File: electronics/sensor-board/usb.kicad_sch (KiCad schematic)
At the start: 1 part

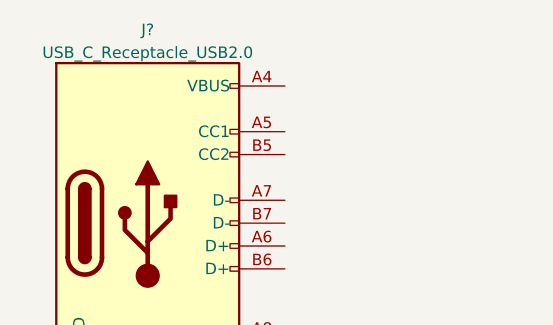
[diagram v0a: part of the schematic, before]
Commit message: Upload power supply schematic
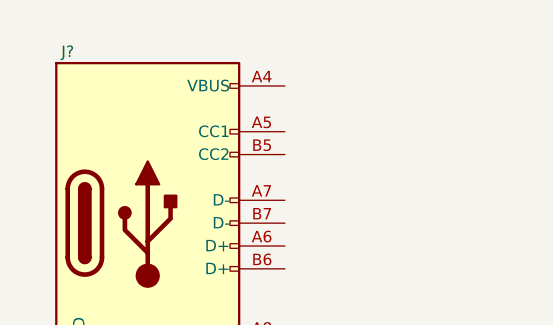
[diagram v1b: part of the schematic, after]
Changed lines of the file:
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@@
   )
   (symbol (lib_id "Connector:USB_C_Receptacle_USB2.0") (at 99.06 76.2 0) (unit 1)
-    (in_bom yes) (on_board yes) (fields_autoplaced)
-    (property "Reference" "J?" (id 0) (at 99.06 54.7202 0))
-    (property "Value" "USB_C_Receptacle_USB2.0" (id 1) (at 99.06 57.2571 0))
+    (in_bom yes) (on_board yes)
+    (property "Reference" "J?" (id 0) (at 90.17 57.15 0))
+    (property "Value" "USB_C_Receptacle_USB2.0" (id 1) (at 99.06 57.2571 0)
+      (effects (font (size 1.27 1.27)) hide)
+    )
     (property "Footprint" "" (id 2) (at 102.87 76.2 0)
       (effects (font (size 1.27 1.27)) hide)

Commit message: Finalize USB
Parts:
- added R?: 1.5k, symbol Device:R_Small
- added R? (x2): 5.1k, symbol Device:R_Small
- added R? (x2): 22R, symbol Device:R_Small
- added TP?: TestPoint, symbol Connector:TestPoint
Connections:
- net USB_DM: now also R?.2
- net USB_DP: now also R?.2
- net GND: now reaches J?.A1 (GND), J?.A12 (GND), J?.B1 (GND), J?.B12 (GND)
- net GND: now also J?.S1 (SHIELD), R?.2, R?.2
- net VBUS: now reaches J?.A4 (VBUS), J?.A9 (VBUS), J?.B4 (VBUS), J?.B9 (VBUS)
- net VBUS: now also TP?.1
- net at J?.A5 (CC1): now also R?.1
- net at J?.A6 (D+): now also J?.B6 (D+), R?.1
- net at J?.A7 (D-): now also J?.B7 (D-), R?.1, R?.1
- net at J?.B5 (CC2): now also R?.1
- new net +3.3V: R?.2
- no-connect marks 0 -> 2
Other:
- note added: "USB for debug, programming and PC data (not a power supply)"
- moved on the sheet: J?

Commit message: Build Pad Bus and annotate
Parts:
- removed TP?: TestPoint, symbol Connector:TestPoint
- gave numbers to parts that had none: 6
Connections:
- net VBUS: no longer names the net of J18.A4 (VBUS), J18.A9 (VBUS), J18.B4 (VBUS), J18.B9 (VBUS)
- no-connect marks 2 -> 3
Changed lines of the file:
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@@
 (kicad_sch (version 20211123) (generator eeschema)
   (paper "A4")
-  (junction (at 52.07 29.21) (diameter 0) (color 0 0 0 0)
-  )
-  (junction (at 60.96 29.21) (diameter 0) (color 0 0 0 0)
-  )
   (junction (at 48.26 41.91) (diameter 0) (color 0 0 0 0)
   )
@@
   (junction (at 48.26 46.99) (diameter 0) (color 0 0 0 0)
   )
+  (no_connect (at 45.72 29.21))
   (no_connect (at 45.72 57.15))
   (no_connect (at 45.72 59.69))
@@
     (stroke (width 0) (type default) (color 0 0 0 0))
   )
-  (wire (pts (xy 52.07 26.67) (xy 52.07 29.21))
-    (stroke (width 0) (type default) (color 0 0 0 0))
-  )
-  (wire (pts (xy 67.31 29.21) (xy 60.96 29.21))
-    (stroke (width 0) (type default) (color 0 0 0 0))
-  )
   (wire (pts (xy 45.72 46.99) (xy 48.26 46.99))
     (stroke (width 0) (type default) (color 0 0 0 0))
@@
     (stroke (width 0) (type default) (color 0 0 0 0))
   )
-  (wire (pts (xy 60.96 29.21) (xy 60.96 26.67))
-    (stroke (width 0) (type default) (color 0 0 0 0))
-  )
-  (wire (pts (xy 67.31 27.94) (xy 67.31 29.21))
-    (stroke (width 0) (type default) (color 0 0 0 0))
-  )
   (wire (pts (xy 48.26 46.99) (xy 48.26 49.53))
     (stroke (width 0) (type default) (color 0 0 0 0))
@@
     (stroke (width 0) (type default) (color 0 0 0 0))
   )
-  (wire (pts (xy 52.07 29.21) (xy 60.96 29.21))
-    (stroke (width 0) (type default) (color 0 0 0 0))
-  )
   (wire (pts (xy 22.86 69.85) (xy 22.86 71.12))
     (stroke (width 0) (type default) (color 0 0 0 0))
@@
   )
   (wire (pts (xy 48.26 49.53) (xy 45.72 49.53))
-    (stroke (width 0) (type default) (color 0 0 0 0))
-  )
-  (wire (pts (xy 45.72 29.21) (xy 52.07 29.21))
     (stroke (width 0) (type default) (color 0 0 0 0))
   )
@@
   (symbol (lib_id "power:GND") (at 72.39 38.1 0) (unit 1)
     (in_bom yes) (on_board yes) (fields_autoplaced)
-    (property "Reference" "#PWR?" (id 0) (at 72.39 44.45 0)
+    (property "Reference" "#PWR0103" (id 0) (at 72.39 44.45 0)
       (effects (font (size 1.27 1.27)) hide)
     )
@@
     (pin "1")
   )
-  (symbol (lib_id "power:VBUS") (at 52.07 26.67 0) (unit 1)
-    (in_bom yes) (on_board yes) (fields_autoplaced)
-    (property "Reference" "#PWR?" (id 0) (at 52.07 30.48 0)
-      (effects (font (size 1.27 1.27)) hide)
-    )
-    (property "Value" "VBUS" (id 1) (at 52.07 23.0942 0))
-    (property "Footprint" "" (id 2) (at 52.07 26.67 0)
-      (effects (font (size 1.27 1.27)) hide)
-    )
-    (property "Datasheet" "" (id 3) (at 52.07 26.67 0)
-      (effects (font (size 1.27 1.27)) hide)
-    )
-    (pin "1")
-  )
   (symbol (lib_id "Device:R_Small") (at 52.07 39.37 90) (unit 1)
     (in_bom yes) (on_board yes)
-    (property "Reference" "R?" (id 0) (at 55.88 40.64 90))
+    (property "Reference" "R56" (id 0) (at 55.88 40.64 90))
     (property "Value" "1.5k" (id 1) (at 57.15 38.1 90))
     (property "Footprint" "" (id 2) (at 52.07 39.37 0)
@@
   (symbol (lib_id "Device:R_Small") (at 52.07 36.83 90) (unit 1)
     (in_bom yes) (on_board yes)
-    (property "Reference" "R?" (id 0) (at 48.26 35.56 90))
+    (property "Reference" "R55" (id 0) (at 48.26 35.56 90))
     (property "Value" "5.1k" (id 1) (at 57.15 35.56 90))
     (property "Footprint" "" (id 2) (at 52.07 36.83 0)
@@
   (symbol (lib_id "power:+3.3V") (at 63.5 38.1 0) (unit 1)
     (in_bom yes) (on_board yes)
-    (property "Reference" "#PWR?" (id 0) (at 63.5 41.91 0)
+    (property "Reference" "#PWR0102" (id 0) (at 63.5 41.91 0)
       (effects (font (size 1.27 1.27)) hide)
     )
@@
     (pin "1")
   )
-  (symbol (lib_id "Connector:TestPoint") (at 67.31 27.94 0) (unit 1)
-    (in_bom yes) (on_board yes) (fields_autoplaced)
-    (property "Reference" "TP?" (id 0) (at 68.707 23.8033 0)
-      (effects (font (size 1.27 1.27)) (justify left))
-    )
-    (property "Value" "TestPoint" (id 1) (at 68.707 26.3402 0)
-      (effects (font (size 1.27 1.27)) (justify left))
-    )
-    (property "Footprint" "" (id 2) (at 72.39 27.94 0)
-      (effects (font (size 1.27 1.27)) hide)
-    )
-    (property "Datasheet" "~" (id 3) (at 72.39 27.94 0)
-      (effects (font (size 1.27 1.27)) hide)
-    )
-    (pin "1")
-  )
   (symbol (lib_id "Connector:USB_C_Receptacle_USB2.0") (at 30.48 44.45 0) (unit 1)
     (in_bom yes) (on_board yes)
-    (property "Reference" "J?" (id 0) (at 21.59 25.4 0))
+    (property "Reference" "J18" (id 0) (at 21.59 25.4 0))
     (property "Value" "USB_C_Receptacle_USB2.0" (id 1) (at 30.48 25.5071 0)
       (effects (font (size 1.27 1.27)) hide)
@@
   (symbol (lib_id "Device:R_Small") (at 52.07 34.29 90) (unit 1)
     (in_bom yes) (on_board yes)
-    (property "Reference" "R?" (id 0) (at 48.26 33.02 90))
+    (property "Reference" "R54" (id 0) (at 48.26 33.02 90))
     (property "Value" "5.1k" (id 1) (at 57.15 33.02 90))
     (property "Footprint" "" (id 2) (at 52.07 34.29 0)
@@
   (symbol (lib_id "power:GND") (at 22.86 71.12 0) (unit 1)
     (in_bom yes) (on_board yes) (fields_autoplaced)
-    (property "Reference" "#PWR?" (id 0) (at 22.86 77.47 0)
+    (property "Reference" "#PWR0101" (id 0) (at 22.86 77.47 0)
       (effects (font (size 1.27 1.27)) hide)
     )
@@
     (pin "1")
   )
-  (symbol (lib_id "power:PWR_FLAG") (at 60.96 26.67 0) (unit 1)
-    (in_bom yes) (on_board yes) (fields_autoplaced)
-    (property "Reference" "#FLG?" (id 0) (at 60.96 24.765 0)
-      (effects (font (size 1.27 1.27)) hide)
-    )
-    (property "Value" "PWR_FLAG" (id 1) (at 60.96 23.0942 0))
-    (property "Footprint" "" (id 2) (at 60.96 26.67 0)
-      (effects (font (size 1.27 1.27)) hide)
-    )
-    (property "Datasheet" "~" (id 3) (at 60.96 26.67 0)
-      (effects (font (size 1.27 1.27)) hide)
-    )
-    (pin "1")
-  )
   (symbol (lib_id "Device:R_Small") (at 52.07 46.99 90) (unit 1)
     (in_bom yes) (on_board yes)
-    (property "Reference" "R?" (id 0) (at 55.88 48.26 90))
+    (property "Reference" "R58" (id 0) (at 55.88 48.26 90))
     (property "Value" "22R" (id 1) (at 52.07 49.53 90))
     (property "Footprint" "" (id 2) (at 52.07 46.99 0)
@@
   (symbol (lib_id "Device:R_Small") (at 52.07 41.91 90) (unit 1)
     (in_bom yes) (on_board yes)
-    (property "Reference" "R?" (id 0) (at 55.88 43.18 90))
+    (property "Reference" "R57" (id 0) (at 55.88 43.18 90))
     (property "Value" "22R" (id 1) (at 52.07 44.45 90))
     (property "Footprint" "" (id 2) (at 52.07 41.91 0)

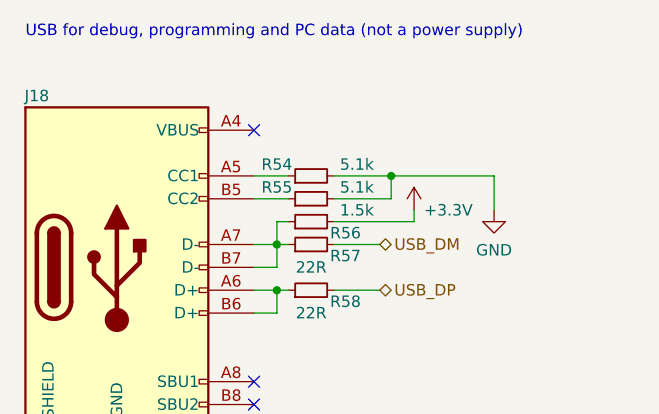
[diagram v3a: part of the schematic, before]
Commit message: Minor tweaks, footprints added
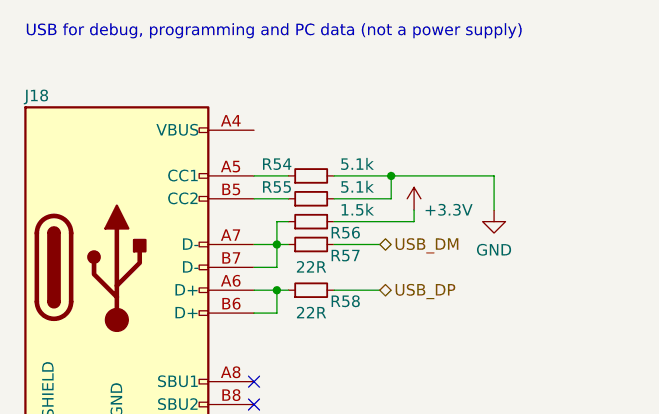
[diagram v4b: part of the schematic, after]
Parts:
- J18: footprint (none) -> Connector_USB:USB_C_Receptacle_Palconn_UTC16-G
- R54, R55, R56, R57, R58: footprint (none) -> Resistor_SMD:R_0603_1608Metric
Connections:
- no-connect marks 3 -> 2
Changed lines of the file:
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@@
   (junction (at 48.26 46.99) (diameter 0) (color 0 0 0 0)
   )
-  (no_connect (at 45.72 29.21))
   (no_connect (at 45.72 57.15))
   (no_connect (at 45.72 59.69))
@@
     (property "Reference" "R56" (id 0) (at 55.88 40.64 90))
     (property "Value" "1.5k" (id 1) (at 57.15 38.1 90))
-    (property "Footprint" "" (id 2) (at 52.07 39.37 0)
+    (property "Footprint" "Resistor_SMD:R_0603_1608Metric" (id 2) (at 52.07 39.37 0)
       (effects (font (size 1.27 1.27)) hide)
     )
@@
     (property "Reference" "R55" (id 0) (at 48.26 35.56 90))
     (property "Value" "5.1k" (id 1) (at 57.15 35.56 90))
-    (property "Footprint" "" (id 2) (at 52.07 36.83 0)
+    (property "Footprint" "Resistor_SMD:R_0603_1608Metric" (id 2) (at 52.07 36.83 0)
       (effects (font (size 1.27 1.27)) hide)
     )
@@
       (effects (font (size 1.27 1.27)) hide)
     )
-    (property "Footprint" "" (id 2) (at 34.29 44.45 0)
+    (property "Footprint" "Connector_USB:USB_C_Receptacle_Palconn_UTC16-G" (id 2) (at 34.29 44.45 0)
       (effects (font (size 1.27 1.27)) hide)
     )
@@
     (property "Reference" "R54" (id 0) (at 48.26 33.02 90))
     (property "Value" "5.1k" (id 1) (at 57.15 33.02 90))
-    (property "Footprint" "" (id 2) (at 52.07 34.29 0)
+    (property "Footprint" "Resistor_SMD:R_0603_1608Metric" (id 2) (at 52.07 34.29 0)
       (effects (font (size 1.27 1.27)) hide)
     )
@@
     (property "Reference" "R58" (id 0) (at 55.88 48.26 90))
     (property "Value" "22R" (id 1) (at 52.07 49.53 90))
-    (property "Footprint" "" (id 2) (at 52.07 46.99 0)
+    (property "Footprint" "Resistor_SMD:R_0603_1608Metric" (id 2) (at 52.07 46.99 0)
       (effects (font (size 1.27 1.27)) hide)
     )
@@
     (property "Reference" "R57" (id 0) (at 55.88 43.18 90))
     (property "Value" "22R" (id 1) (at 52.07 44.45 90))
-    (property "Footprint" "" (id 2) (at 52.07 41.91 0)
-      (effects (font (size 1.27 1.27)) hide)
-    )
+    (property "Footprint" "Resistor_SMD:R_0603_1608Metric" (id 2) (at 52.07 41.91 0)
+      (effects (font (size 1.27 1.27)) hide)
+    )

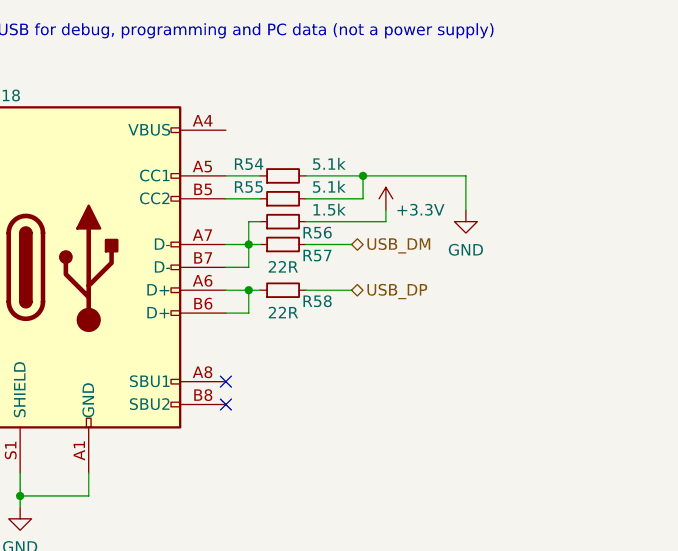
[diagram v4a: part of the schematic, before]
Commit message: Set up board rules w/ controlled impedance
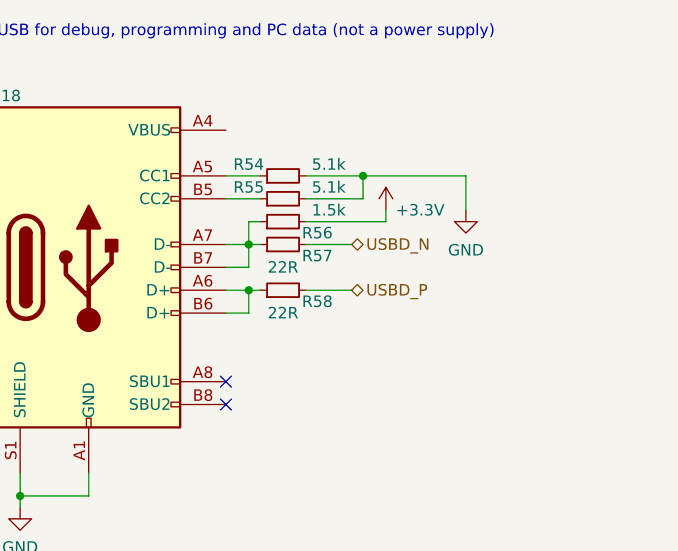
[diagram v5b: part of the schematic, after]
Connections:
- net USB_DM renamed USBD_N
- net USB_DP renamed USBD_P
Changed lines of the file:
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@@
     (effects (font (size 1.27 1.27)) (justify left bottom))
   )
-  (hierarchical_label "USB_DM" (shape bidirectional) (at 59.69 41.91 0)
+  (hierarchical_label "USBD_N" (shape bidirectional) (at 59.69 41.91 0)
     (effects (font (size 1.27 1.27)) (justify left))
   )
-  (hierarchical_label "USB_DP" (shape bidirectional) (at 59.69 46.99 0)
+  (hierarchical_label "USBD_P" (shape bidirectional) (at 59.69 46.99 0)
     (effects (font (size 1.27 1.27)) (justify left))
   )

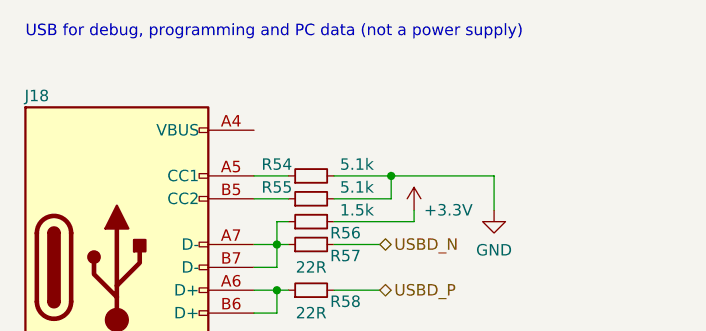
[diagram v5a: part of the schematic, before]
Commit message: Remove DIP switches and re-organize CAN connectors
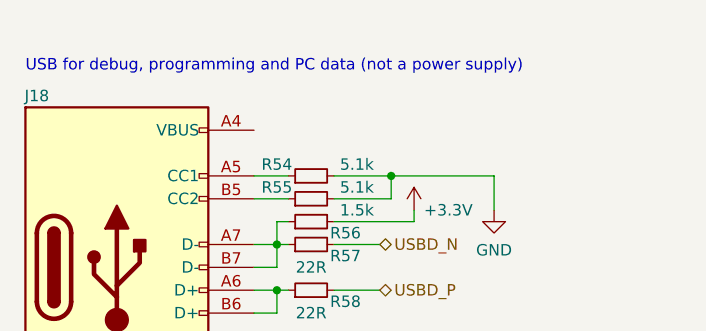
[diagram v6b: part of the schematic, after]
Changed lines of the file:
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@@
   )
   (text "USB for debug, programming and PC data (not a power supply)"
-    (at 20.32 19.05 0)
+    (at 20.32 22.86 0)
     (effects (font (size 1.27 1.27)) (justify left bottom))
   )

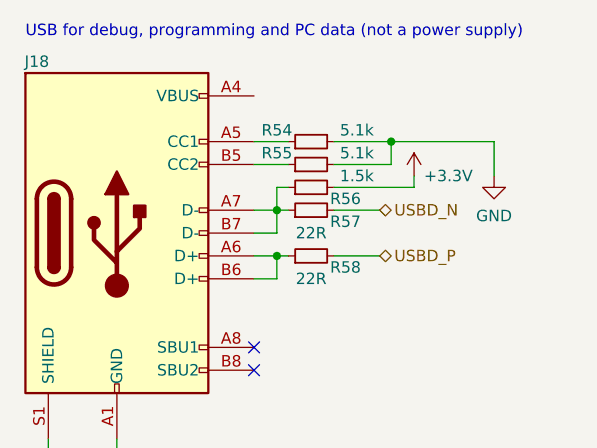
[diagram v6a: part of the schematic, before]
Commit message: Update reference designators
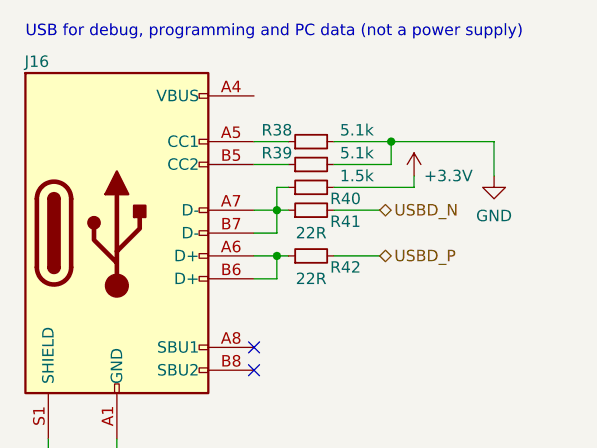
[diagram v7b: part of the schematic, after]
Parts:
- renumbered J18 to J16, R54 to R38, R55 to R39, R56 to R40, R57 to R41, R58 to R42
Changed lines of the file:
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@@
   (symbol (lib_id "power:GND") (at 72.39 38.1 0) (unit 1)
     (in_bom yes) (on_board yes) (fields_autoplaced)
-    (property "Reference" "#PWR0103" (id 0) (at 72.39 44.45 0)
+    (property "Reference" "#PWR095" (id 0) (at 72.39 44.45 0)
       (effects (font (size 1.27 1.27)) hide)
     )
@@
   (symbol (lib_id "Device:R_Small") (at 52.07 39.37 90) (unit 1)
     (in_bom yes) (on_board yes)
-    (property "Reference" "R56" (id 0) (at 55.88 40.64 90))
+    (property "Reference" "R40" (id 0) (at 55.88 40.64 90))
     (property "Value" "1.5k" (id 1) (at 57.15 38.1 90))
     (property "Footprint" "Resistor_SMD:R_0603_1608Metric" (id 2) (at 52.07 39.37 0)
@@
   (symbol (lib_id "Device:R_Small") (at 52.07 36.83 90) (unit 1)
     (in_bom yes) (on_board yes)
-    (property "Reference" "R55" (id 0) (at 48.26 35.56 90))
+    (property "Reference" "R39" (id 0) (at 48.26 35.56 90))
     (property "Value" "5.1k" (id 1) (at 57.15 35.56 90))
     (property "Footprint" "Resistor_SMD:R_0603_1608Metric" (id 2) (at 52.07 36.83 0)
@@
   (symbol (lib_id "power:+3.3V") (at 63.5 38.1 0) (unit 1)
     (in_bom yes) (on_board yes)
-    (property "Reference" "#PWR0102" (id 0) (at 63.5 41.91 0)
+    (property "Reference" "#PWR094" (id 0) (at 63.5 41.91 0)
       (effects (font (size 1.27 1.27)) hide)
     )
@@
   (symbol (lib_id "Connector:USB_C_Receptacle_USB2.0") (at 30.48 44.45 0) (unit 1)
     (in_bom yes) (on_board yes)
-    (property "Reference" "J18" (id 0) (at 21.59 25.4 0))
+    (property "Reference" "J16" (id 0) (at 21.59 25.4 0))
     (property "Value" "USB_C_Receptacle_USB2.0" (id 1) (at 30.48 25.5071 0)
       (effects (font (size 1.27 1.27)) hide)
@@
   (symbol (lib_id "Device:R_Small") (at 52.07 34.29 90) (unit 1)
     (in_bom yes) (on_board yes)
-    (property "Reference" "R54" (id 0) (at 48.26 33.02 90))
+    (property "Reference" "R38" (id 0) (at 48.26 33.02 90))
     (property "Value" "5.1k" (id 1) (at 57.15 33.02 90))
     (property "Footprint" "Resistor_SMD:R_0603_1608Metric" (id 2) (at 52.07 34.29 0)
@@
   (symbol (lib_id "power:GND") (at 22.86 71.12 0) (unit 1)
     (in_bom yes) (on_board yes) (fields_autoplaced)
-    (property "Reference" "#PWR0101" (id 0) (at 22.86 77.47 0)
+    (property "Reference" "#PWR093" (id 0) (at 22.86 77.47 0)
       (effects (font (size 1.27 1.27)) hide)
     )
@@
   (symbol (lib_id "Device:R_Small") (at 52.07 46.99 90) (unit 1)
     (in_bom yes) (on_board yes)
-    (property "Reference" "R58" (id 0) (at 55.88 48.26 90))
+    (property "Reference" "R42" (id 0) (at 55.88 48.26 90))
     (property "Value" "22R" (id 1) (at 52.07 49.53 90))
     (property "Footprint" "Resistor_SMD:R_0603_1608Metric" (id 2) (at 52.07 46.99 0)
@@
   (symbol (lib_id "Device:R_Small") (at 52.07 41.91 90) (unit 1)
     (in_bom yes) (on_board yes)
-    (property "Reference" "R57" (id 0) (at 55.88 43.18 90))
+    (property "Reference" "R41" (id 0) (at 55.88 43.18 90))
     (property "Value" "22R" (id 1) (at 52.07 44.45 90))
     (property "Footprint" "Resistor_SMD:R_0603_1608Metric" (id 2) (at 52.07 41.91 0)

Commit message: Further PCB layout
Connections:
- net USB_N: now reaches J16.A7 (D-), J16.B7 (D-), R40.1, R41.1
- net USB_P: now reaches J16.A6 (D+), J16.B6 (D+), R42.1
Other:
- moved on the sheet: R38, R39, R40, R41, R42
